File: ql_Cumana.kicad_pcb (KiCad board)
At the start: 2 copper layers, 129.5 x 101.6 mm, 40 parts, among them J1 QL_SLOT_DIN41612_CARD, J2 Conn_02x17_Odd_Even, U1 LS04, U10 74LS273, U11 74LS133, U12 FDC_WD1772, U13 27C128, U14 74LS245, U2 7805, U3 LS00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

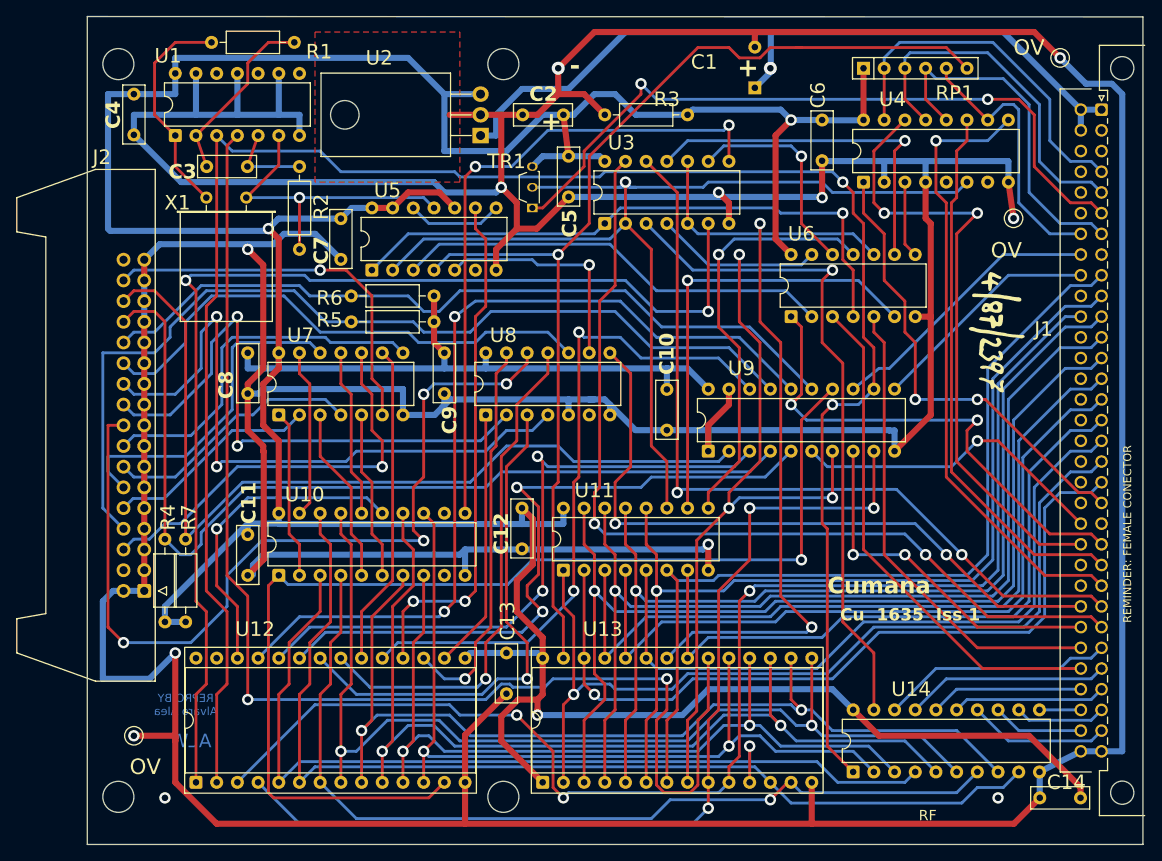
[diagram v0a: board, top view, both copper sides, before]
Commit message: update component values
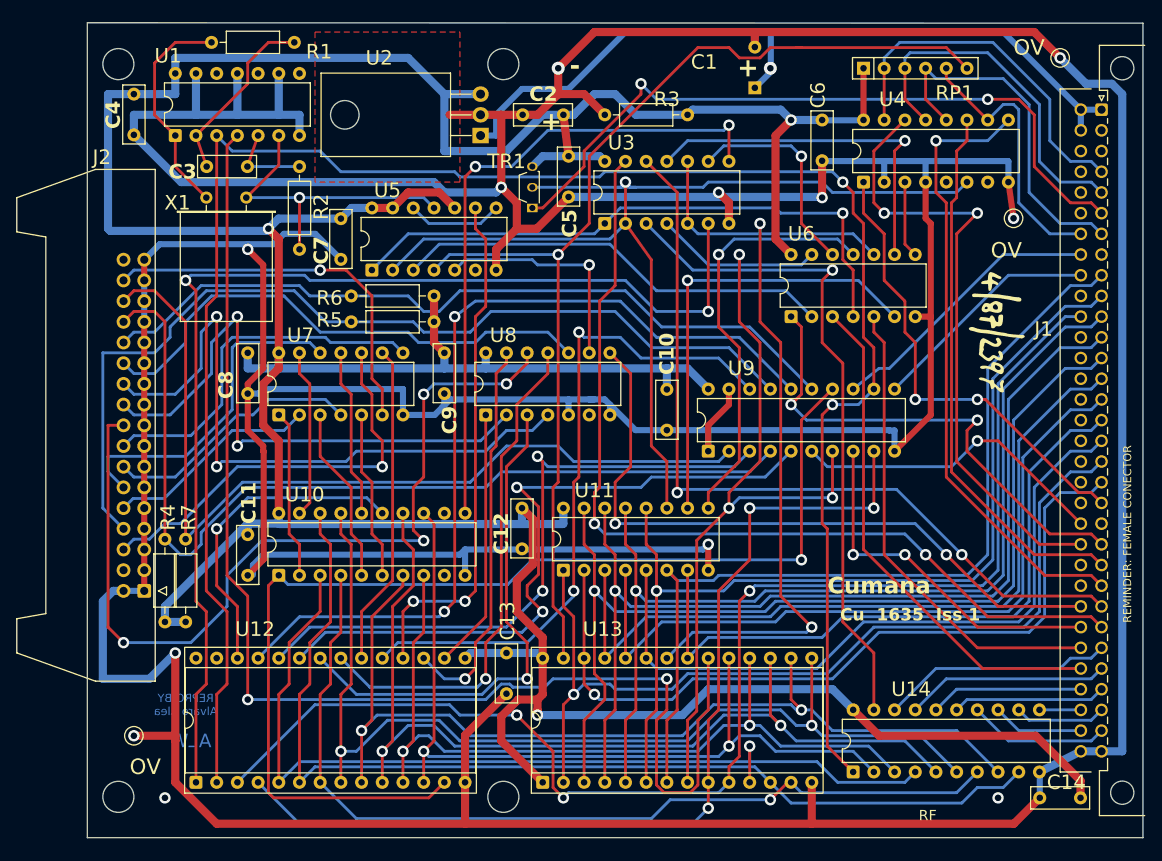
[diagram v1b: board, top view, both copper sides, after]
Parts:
- R2: value 3K7 -> 4K7
- TR1: value BC2369 -> 2N2369
- U1: value LS04 -> 74LS04
- U3: value LS00 -> 74LS00
- U7, U8: value 74LS16 -> 74LS06
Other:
- board size 129.5 x 101.6 mm -> 129.5 x 100 mm
